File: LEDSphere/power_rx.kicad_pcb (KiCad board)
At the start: 2 copper layers, 140 x 140 mm, 47 parts, among them U114 DRV5033FAQDBZR, U3 TPS54202HDDCR, U4 TPS54202HDDCR

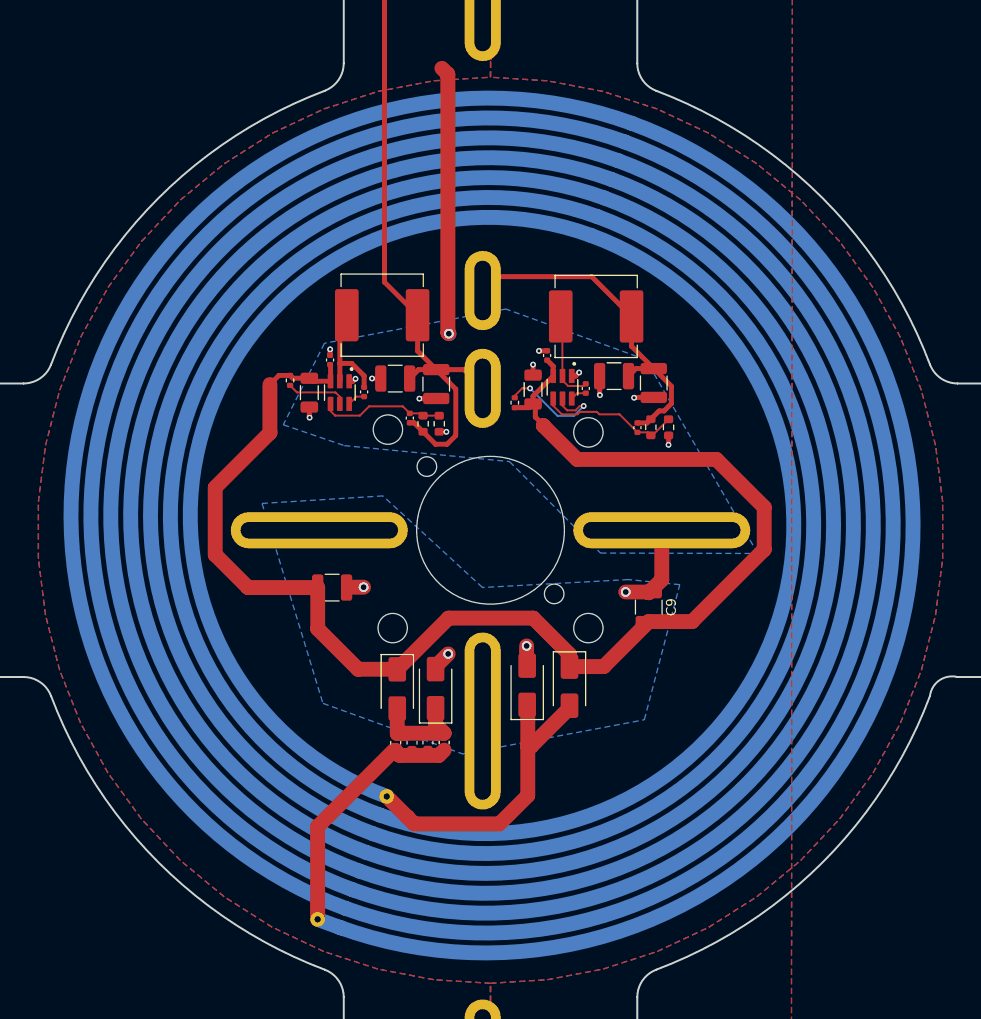
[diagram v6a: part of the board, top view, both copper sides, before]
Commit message: change power rx gnding, add step files of all boards
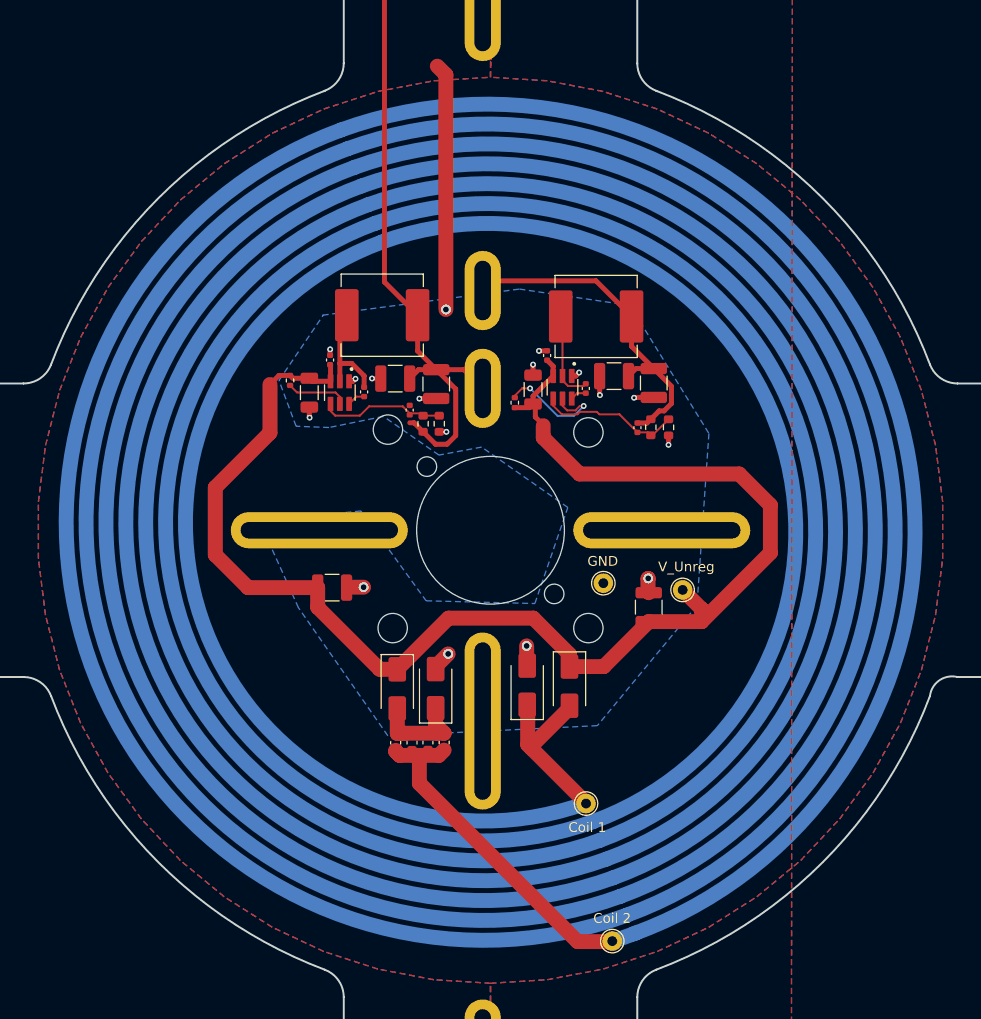
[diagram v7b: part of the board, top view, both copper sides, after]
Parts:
- added Coil 1: Coil1, TestPoint:TestPoint_THTPad_D2.0mm_Drill1.0mm, F.Cu at (104.2, 132.2)
- added Coil 2: Coil2, TestPoint:TestPoint_THTPad_D2.0mm_Drill1.0mm, F.Cu at (106.9, 146.3)
- added GND: GND, TestPoint:TestPoint_THTPad_D2.0mm_Drill1.0mm, F.Cu at (106.0, 109.7)
- added TP3: CoilOut, TestPoint:TestPoint_THTPad_D2.0mm_Drill1.0mm, F.Cu at (114.1, 110.4)
- moved REF** 0.84 mm to (93.8, 103.5), turned to -70 degrees
- moved C17 0.82 mm to (86.2, 92.0)
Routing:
- net /coil1: track 32.2 -> 18.5 mm
- net GND: track 55.8 -> 45.8 mm
- net /coil2: track 26.0 -> 34.7 mm
- net /U_unreg: track 142.2 -> 147.3 mm
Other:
- board text added: "V_Unreg"

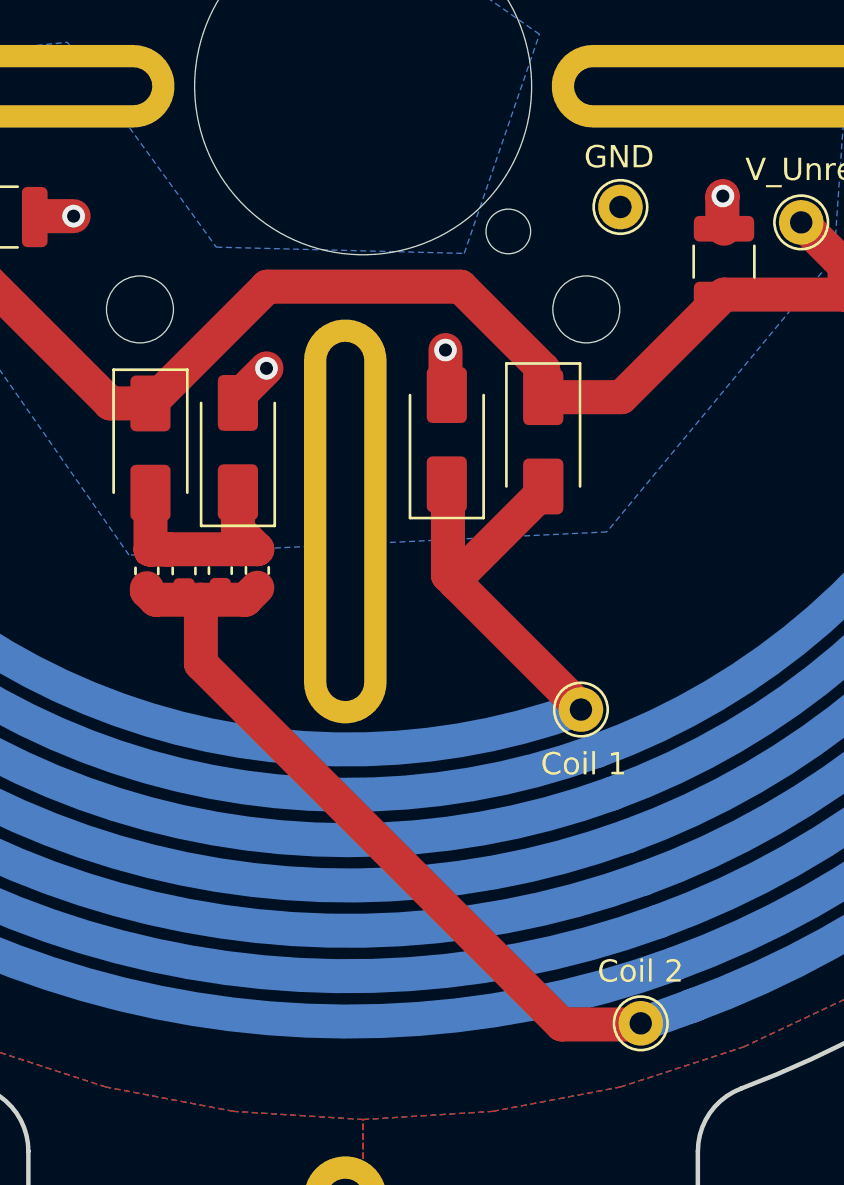
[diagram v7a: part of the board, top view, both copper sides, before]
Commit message: adjust test point
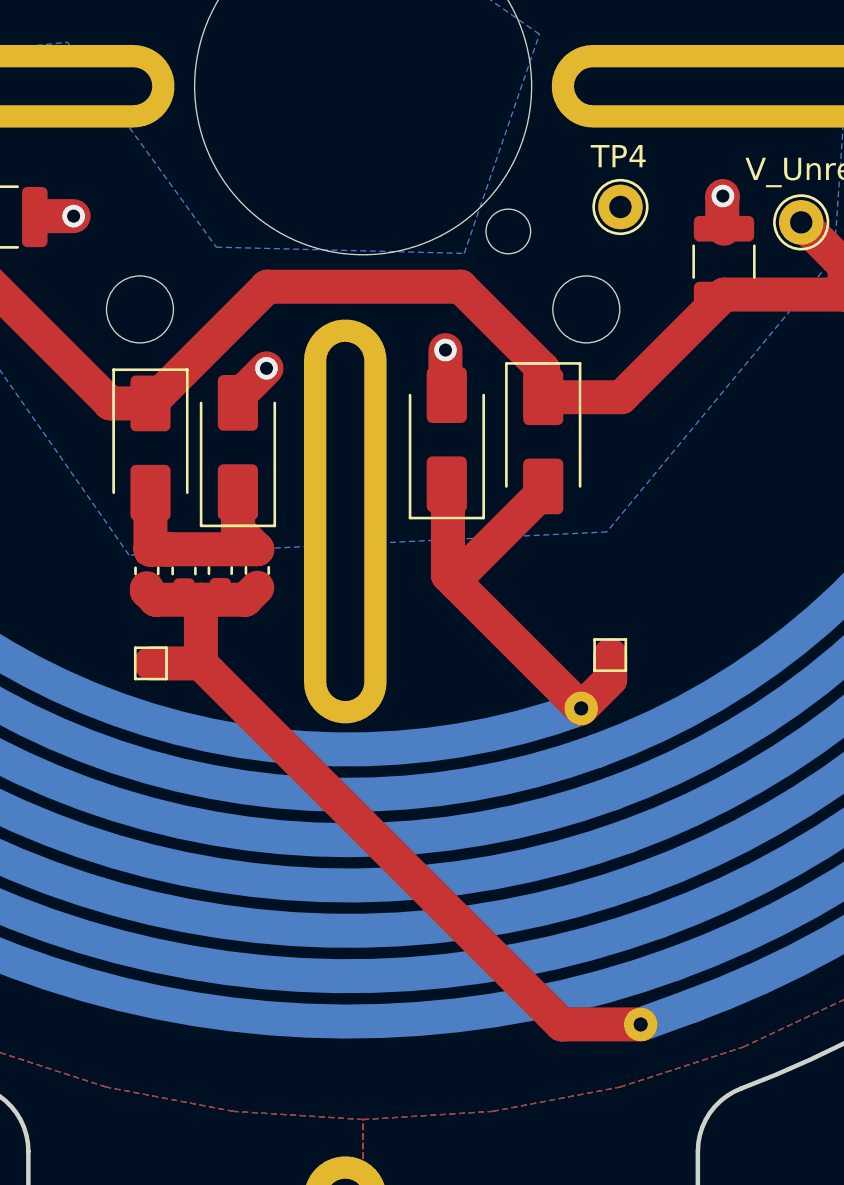
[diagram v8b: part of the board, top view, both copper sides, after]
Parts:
- removed Coil 1: Coil1, TestPoint:TestPoint_THTPad_D2.0mm_Drill1.0mm
- removed Coil 2: Coil2, TestPoint:TestPoint_THTPad_D2.0mm_Drill1.0mm
- added TP1: Coil2, TestPoint:TestPoint_Pad_1.0x1.0mm, F.Cu at (85.0, 130.1)
- added TP2: Coil1, TestPoint:TestPoint_Pad_1.0x1.0mm, F.Cu at (105.6, 129.8)
- renumbered GND to TP4
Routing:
- net /coil1: track 18.5 -> 21.4 mm
- net /coil2: track 34.7 -> 37.0 mm
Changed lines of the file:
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@@
 		)
 	)
+	(footprint "TestPoint:TestPoint_Pad_1.0x1.0mm"
+		(layer "F.Cu")
+		(at 84.98 130.14 -90)
+		(descr "SMD rectangular pad as test Point, square 1.0mm side length")
+		(tags "test point SMD pad rectangle square")
+		(property "Reference" "TP1"
+			(at 0 -1.448 90)
+			(layer "F.SilkS")
+			(hide yes)
+			(effects
+				(font
+					(size 1 1)
+					(thickness 0.15)
+				)
+			)
+		)
+		(property "Value" "Coil2"
+			(at 0 1.55 90)
+			(layer "F.Fab")
+			(effects
+				(font
+					(size 1 1)
+					(thickness 0.15)
+				)
+			)
+		)
+		(property "Datasheet" ""
+			(at 0 0 270)
+			(unlocked yes)
+			(layer "F.Fab")
+			(hide yes)
+			(effects
+				(font
+					(size 1.27 1.27)
+					(thickness 0.15)
+				)
+			)
+		)
+		(property "Description" "test point"
+			(at 0 0 270)
+			(unlocked yes)
+			(layer "F.Fab")
+			(hide yes)
+			(effects
+				(font
+					(size 1.27 1.27)
+					(thickness 0.15)
+				)
+			)
+		)
+		(property ki_fp_filters "Pin* Test*")
+		(sheetname "/")
+		(sheetfile "power_rx.kicad_sch")
+		(units
+			(unit
+				(name "A")
+				(pins "1")
+			)
+		)
+		(duplicate_pad_numbers_are_jumpers no)
+		(fp_line
+			(start -0.7 0.7)
+			(end -0.7 -0.7)
+			(stroke
+				(width 0.12)
+				(type solid)
+			)
+			(layer "F.SilkS")
+		)
+		(fp_line
+			(start 0.7 0.7)
+			(end -0.7 0.7)
+			(stroke
+				(width 0.12)
+				(type solid)
+			)
+			(layer "F.SilkS")
+		)
+		(fp_line
+			(start -0.7 -0.7)
+			(end 0.7 -0.7)
+			(stroke
+				(width 0.12)
+				(type solid)
+			)
+			(layer "F.SilkS")
+		)
+		(fp_line
+			(start 0.7 -0.7)
+			(end 0.7 0.7)
+			(stroke
+				(width 0.12)
+				(type solid)
+			)
+			(layer "F.SilkS")
+		)
+		(fp_line
+			(start 1 1)
+			(end -1 1)
+			(stroke
+				(width 0.05)
+				(type solid)
+			)
+			(layer "F.CrtYd")
+		)
+		(fp_line
+			(start 1 1)
+			(end 1 -1)
+			(stroke
+				(width 0.05)
+				(type solid)
+			)
+			(layer "F.CrtYd")
+		)
+		(fp_line
+			(start -1 -1)
+			(end -1 1)
+			(stroke
+				(width 0.05)
+				(type solid)
+			)
+			(layer "F.CrtYd")
+		)
+		(fp_line
+			(start -1 -1)
+			(end 1 -1)
+			(stroke
+				(width 0.05)
+				(type solid)
+			)
+			(layer "F.CrtYd")
+		)
+		(fp_text user "${REFERENCE}"
+			(at 0 -1.45 90)
+			(layer "F.Fab")
+			(effects
+				(font
+					(size 1 1)
+					(thickness 0.15)
+				)
+			)
+		)
+		(pad "1" smd rect
+			(at 0 0 270)
+			(size 1 1)
+			(layers "F.Cu" "F.Mask")
+			(net "/coil2")
+			(pinfunction "1_1")
+			(pintype "passive")
+		)
+		(embedded_fonts no)
+	)
 	(footprint "Resistor_SMD:R_0603_1608Metric"
 		(layer "F.Cu")
@@
 		)
 	)
-	(footprint "TestPoint:TestPoint_THTPad_D2.0mm_Drill1.0mm"
-		(layer "F.Cu")
-		(at 104.25 132.21)
-		(descr "THT pad as test Point, diameter 2.0mm, hole diameter 1.0mm")
-		(tags "test point THT pad")
-		(property "Reference" "Coil 1"
-			(at 0.13 2.44 0)
-			(layer "F.SilkS")
-			(effects
-				(font
-					(size 1 1)
-					(thickness 0.15)
-				)
-			)
-		)
-		(property "Value" "Coil1"
-			(at 0 2.05 0)
-			(layer "F.Fab")
-			(effects
-				(font
-					(size 1 1)
-					(thickness 0.15)
-				)
-			)
-		)
-		(property "Datasheet" ""
-			(at 0 0 0)
-			(unlocked yes)
-			(layer "F.Fab")
-			(hide yes)
-			(effects
-				(font
-					(size 1.27 1.27)
-					(thickness 0.15)
-				)
-			)
-		)
-		(property "Description" "test point"
-			(at 0 0 0)
-			(unlocked yes)
-			(layer "F.Fab")
-			(hide yes)
-			(effects
-				(font
-					(size 1.27 1.27)
-					(thickness 0.15)
-				)
-			)
-		)
-		(property ki_fp_filters "Pin* Test*")
-		(sheetname "/")
-		(sheetfile "power_rx.kicad_sch")
-		(units
-			(unit
-				(name "A")
-				(pins "1")
-			)
-		)
-		(duplicate_pad_numbers_are_jumpers no)
-		(fp_circle
-			(center 0 0)
-			(end 0 1.2)
-			(stroke
-				(width 0.12)
-				(type solid)
-			)
-			(fill no)
-			(layer "F.SilkS")
-		)
-		(fp_circle
-			(center 0 0)
-			(end 1.5 0)
-			(stroke
-				(width 0.05)
-				(type solid)
-			)
-			(fill no)
-			(layer "F.CrtYd")
-		)
-		(fp_text user "${REFERENCE}"
-			(at 0 -2 0)
-			(layer "F.Fab")
-			(effects
-				(font
-					(size 1 1)
-					(thickness 0.15)
-				)
-			)
-		)
-		(pad "1" thru_hole circle
-			(at 0 0)
-			(size 2 2)
-			(drill 1)
-			(layers "*.Cu" "*.Mask")
-			(remove_unused_layers no)
-			(net "/coil1")
-			(pinfunction "1_1")
-			(pintype "passive")
-		)
-		(embedded_fonts no)
-	)
 	(footprint "my_footprints:slot_short"
 		(layer "F.Cu")
@@
 		(descr "THT pad as test Point, diameter 2.0mm, hole diameter 1.0mm")
 		(tags "test point THT pad")
-		(property "Reference" "GND"
+		(property "Reference" "TP4"
 			(at -0.06 -2.24 0)
 			(layer "F.SilkS")
@@
 		(embedded_fonts no)
 	)
-	(footprint "TestPoint:TestPoint_THTPad_D2.0mm_Drill1.0mm"
+	(footprint "TestPoint:TestPoint_Pad_1.0x1.0mm"
 		(layer "F.Cu")
-		(at 106.93 146.27)
-		(descr "THT pad as test Point, diameter 2.0mm, hole diameter 1.0mm")
-		(tags "test point THT pad")
-		(property "Reference" "Coil 2"
-			(at -0.01 -2.33 0)
+		(at 105.56 129.77)
+		(descr "SMD rectangular pad as test Point, square 1.0mm side length")
+		(tags "test point SMD pad rectangle square")
+		(property "Reference" "TP2"
+			(at 0 -1.448 0)
 			(layer "F.SilkS")
+			(hide yes)
 			(effects
 				(font
@@
 			)
 		)
-		(property "Value" "Coil2"
-			(at 0 2.05 0)
+		(property "Value" "Coil1"
+			(at 0 1.55 0)
 			(layer "F.Fab")
 			(effects
@@
 		)
 		(duplicate_pad_numbers_are_jumpers no)
-		(fp_circle
-			(center 0 0)
-			(end 0 1.2)
+		(fp_line
+			(start -0.7 -0.7)
+			(end 0.7 -0.7)
 			(stroke
 				(width 0.12)
 				(type solid)
 			)
-			(fill no)
 			(layer "F.SilkS")
 		)
-		(fp_circle
-			(center 0 0)
-			(end 1.5 0)
+		(fp_line
+			(start -0.7 0.7)
+			(end -0.7 -0.7)
+			(stroke
+				(width 0.12)
+				(type solid)
+			)
+			(layer "F.SilkS")
+		)
+		(fp_line
+			(start 0.7 -0.7)
+			(end 0.7 0.7)
+			(stroke
+				(width 0.12)
+				(type solid)
+			)
+			(layer "F.SilkS")
+		)
+		(fp_line
+			(start 0.7 0.7)
+			(end -0.7 0.7)
+			(stroke
+				(width 0.12)
+				(type solid)
+			)
+			(layer "F.SilkS")
+		)
+		(fp_line
+			(start -1 -0.999999)
+			(end -0.999999 1)
+			(stroke
+				(width 0.05)
+				(type solid)
+			)
+			(layer "F.CrtYd")
+		)
+		(fp_line
+			(start -1 -0.999999)
+			(end 0.999999 -1)
+			(stroke
+				(width 0.05)
+				(type solid)
+			)
+			(layer "F.CrtYd")
+		)
+		(fp_line
+			(start 1 0.999999)
+			(end -0.999999 1)
+			(stroke
+				(width 0.05)
+				(type solid)
+			)
+			(layer "F.CrtYd")
+		)
+		(fp_line
+			(start 1 0.999999)
+			(end 0.999999 -1)
 			(stroke
 				(width 0.05)
 				(type solid)
 			)
-			(fill no)
 			(layer "F.CrtYd")
 		)
 		(fp_text user "${REFERENCE}"
-			(at 0 -2 0)
+			(at 0 -1.45 0)
 			(layer "F.Fab")
 			(effects
@@
 			)
 		)
-		(pad "1" thru_hole circle
+		(pad "1" smd rect
 			(at 0 0)
-			(size 2 2)
-			(drill 1)
-			(layers "*.Cu" "*.Mask")
-			(remove_unused_layers no)
-			(net "/coil2")
+			(size 1 1)
+			(layers "F.Cu" "F.Mask")
+			(net "/coil1")
 			(pinfunction "1_1")
 			(pintype "passive")
@@
 	)
 	(segment
+		(start 87.21 130.14)
+		(end 87.22 130.15)
+		(width 1.524)
+		(layer "F.Cu")
+		(net "/coil2")
+	)
+	(segment
 		(start 103.390815 146.320815)
 		(end 87.22 130.15)
@@
 	)
 	(segment
+		(start 84.98 130.14)
+		(end 87.21 130.14)
+		(width 1.524)
+		(layer "F.Cu")
+		(net "/coil2")
+	)
+	(segment
 		(start 89.21 127.29)
 		(end 89.75 126.75)
@@
 		(width 1.524)
 		(layer "F.Cu")
+		(net "/coil1")
+	)
+	(segment
+		(start 105.56 129.77)
+		(end 105.56 130.860744)
+		(width 1.524)
+		(layer "F.Cu")
+		(net "/coil1")
+	)
+	(segment
+		(start 105.56 130.860744)
+		(end 104.262686 132.158058)
+		(width 1.524)
+		(layer "F.Cu")
